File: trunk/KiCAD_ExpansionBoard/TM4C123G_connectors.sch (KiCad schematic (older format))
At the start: 0 parts

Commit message: Creation of project (sheets) structure and add some library schematic component (transceiver.lib, headers, etc.)
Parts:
- added J1: TI_BOOSTER_40_J1, ~, symbol TI_BOOSTER_40_J1
- added J2: TI_BOOSTER_40_J2, ~, symbol TI_BOOSTER_40_J2
- added J3: TI_BOOSTER_40_J3, ~, symbol TI_BOOSTER_40_J3
- added J4: TI_BOOSTER_40_J4, ~, symbol TI_BOOSTER_40_J4
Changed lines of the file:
@@
 EESchema Schematic File Version 2
+LIBS:boosterpack
 LIBS:power
 LIBS:device
@@
 LIBS:contrib
 LIBS:valves
+LIBS:transceiver
 LIBS:TM4C123G_CommExpBoard-cache
 EELAYER 27 0
@@
 Date "9 jun 2014"
 Rev "0.1"
-Comp "Luca Buccolini, student @ Università Politecnica delle Marche"
+Comp "Luca Buccolini, Student @ Università Politecnica delle Marche"
 Comment1 "Expansion Board for the Texas Instruments TM4C123G Launchpad "
 Comment2 ""
@@
 Comment4 ""
 $EndDescr
+$Comp
+L TI_BOOSTER_40_J1 J1
+U 1 1 5395F11E
+P 10400 1300
+F 0 "J1" H 10350 1950 60  0000 C CNN
+F 1 "TI_BOOSTER_40_J1" H 10400 650 60  0000 C CNN
+F 2 "~" H 10400 1300 60  0000 C CNN
+F 3 "http://www.farnell.com/datasheets/1662126.pdf" H 10400 1300 60  0001 C CNN
+F 4 "Farnell" H 10400 1300 60  0001 C CNN "Supplier 1"
+F 5 "1593464" H 10400 1300 60  0001 C CNN "Supplier 1 P/N"
+F 6 "Multicomp" H 10400 1300 60  0001 C CNN "Producer"
+F 7 "2212S-10SG-85" H 10400 1300 60  0001 C CNN "Producer P/N"
+	1    10400 1300
+	1    0    0    -1
+$EndComp
+$Comp
+L TI_BOOSTER_40_J2 J2
+U 1 1 5395F12D
+P 10400 2900
+F 0 "J2" H 10350 3550 60  0000 C CNN
+F 1 "TI_BOOSTER_40_J2" H 10400 2250 60  0000 C CNN
+F 2 "~" H 10400 2900 60  0000 C CNN
+F 3 "http://www.farnell.com/datasheets/1662126.pdf" H 10400 2900 60  0001 C CNN
+F 4 "Farnell" H 10400 2900 60  0001 C CNN "Supplier 1"
+F 5 "1593464" H 10400 2900 60  0001 C CNN "Supplier 1 P/N"
+F 6 "Multicomp" H 10400 2900 60  0001 C CNN "Producer"
+F 7 "2212S-10SG-85" H 10400 2900 60  0001 C CNN "Producer P/N"
+	1    10400 2900
+	1    0    0    -1
+$EndComp
+$Comp
+L TI_BOOSTER_40_J3 J3
+U 1 1 5395F13C
+P 10400 4550
+F 0 "J3" H 10350 5200 60  0000 C CNN
+F 1 "TI_BOOSTER_40_J3" H 10400 3900 60  0000 C CNN
+F 2 "~" H 10400 4550 60  0000 C CNN
+F 3 "http://www.farnell.com/datasheets/1662126.pdf" H 10400 4550 60  0001 C CNN
+F 4 "Farnell" H 10400 4550 60  0001 C CNN "Supplier 1"
+F 5 "1593464" H 10400 4550 60  0001 C CNN "Supplier 1 P/N"
+F 6 "Multicomp" H 10400 4550 60  0001 C CNN "Producer"
+F 7 "2212S-10SG-85" H 10400 4550 60  0001 C CNN "Producer P/N"
+	1    10400 4550
+	1    0    0    -1
+$EndComp
+$Comp
+L TI_BOOSTER_40_J4 J4
+U 1 1 5395F14B
+P 10400 6150
+F 0 "J4" H 10350 6800 60  0000 C CNN
+F 1 "TI_BOOSTER_40_J4" H 10400 5500 60  0000 C CNN
+F 2 "~" H 10400 6150 60  0000 C CNN
+F 3 "http://www.farnell.com/datasheets/1662126.pdf" H 10400 6150 60  0001 C CNN
+F 4 "Farnell" H 10400 6150 60  0001 C CNN "Supplier 1"
+F 5 "1593464" H 10400 6150 60  0001 C CNN "Supplier 1 P/N"
+F 6 "Multicomp" H 10400 6150 60  0001 C CNN "Producer "
+F 7 "2212S-10SG-85" H 10400 6150 60  0001 C CNN "Producer P/N"
+	1    10400 6150
+	1    0    0    -1
+$EndComp
 $EndSCHEMATC

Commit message: Circuit board schematic complete! TODO: Update schematic according new received specifics: "note-expansionboard_20140623.txt"
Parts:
- added C5: 10n, ~, symbol C
- added C6, C7: 1n, ~, symbol C
- added P10: EB_GPIO0, symbol CONN_4X2
- added P6: CAN, symbol CONN_4
- added P7: UART1, symbol CONN_3X2
- added P8: RS485, symbol CONN_4
- added P9: UART2, symbol CONN_3X2
- added Q2: TSM3457, SOT-26_MD, symbol MOS_P
- added R19: 15k, ~, symbol R
- added R20, R23, R24, R25, R26: 4k7, ~, symbol R
- added R21, R22: 22, ~, symbol R
- added TVS3: SMCJ12CA, DO-214AB_MD, symbol TVS
- J1, J2, J3: Supplier 2 (none) -> Taydaelectronics; Supplier 2 P/N (none) -> A-1053
- J4: Producer (none) -> Multicomp; Producer  Multicomp -> (none); Supplier 2 (none) -> Taydaelectronics; Supplier 2 P/N (none) -> A-1053
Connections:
- net labels added: +12V_BUS, +12V_BUS_UNP, +3.3V_EB, +3.3V_TLP, +5V_TLP, AIN0, AIN1, CAN0_EN, CAN0_RS, CAN0_RX, CAN0_TX, CAN_H, CAN_L, EXT_AIN0, EXT_AIN1, GND, I2C0_SCL, I2C0_SDA, I2C1_SCL, I2C1_SDA, LED_B, LED_G, LED_R, RESET, RFM_CLK, RFM_GPIO0, RFM_GPIO1, RFM_MISO, RFM_MOSI, RFM_NIRQ, RFM_SCLK, RFM_SDN, RFM_SSEL, RS485_A, RS485_B, RS485_RXEN#, RS485_TXEN, SW1, SW2, UART1_CTS, UART1_RTS, UART1_RX, UART1_TX, UART2_RST, UART2_RX, UART2_TREQ, UART2_TX, UART3_RX, UART3_TX, V_AN_MONITOR
- wire segments 0 -> 114
- no-connect marks 0 -> 6
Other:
- note added: "4x Stackable 10 pin headers"
- note added: "ADC input: generic \nanti-aliasing filter"
- note added: "CAN connector & \npower supply rail"
- note added: "Divider ratio=0.2541\n"
- note added: "I2C: generic \npull-up resistor"
- note added: "RS-485 connector &\npower supply rail"
- note added: "Spare function 4x2 male header"
- note added: "Transient & reverse polarity protections\nof power supply rail\n"
- note added: "UART1 3x2 male header"
- note added: "UART2 3x2 male header"
- note added: "if order skackable 10 pins header, \nyou can remove the four I2C pins \non this header (EB_GPIO0)"

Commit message: -Unito le due linee a 3.3V e riposizionato Q1 che ora va ad interrompere la linea di alimentazione a 3.3V dello switching quando è presente la +5V_TLP (USB). In serie al gate ho messo R8 da 120 ohm e ho lasciato R7 da 10k di pull-down.
-Ho messo un NPN, Q3, che ha al suo interno un partitore da 22k + 47k; è pilotato dalla +5V_TLP ed ho messo R1 verso +12V_BUS che mantiene attivo lo switching a meno che non sia presente la +5V_TLP (Q3 ON). Infine ho posizionato il led a monte del PMOS.

-Per la protezione dalle sovratensioni sulla +5V_TLP ho inserito, all'ingesso, TVS4 che è bidirezionale con tensione di lavoro a 5V e tensione di breakdown di 5.8V (min).

-Rimosse tutte le resistenze di pull-up nei transceiver: ne avevano alcune già internamente.

-Sostituiti gli header-jumper per i terminatori e la rete di fail-safe biasing con un SPDT (SW1), ed un 4PDT (SW2).

In serie al pin RS del transceiver ho messo una 10k.

Pull-up da 10k su SDN dell'RF module
 
Ho inserito un secondo TP P1, ANT_GND che posizionerò vicino al primo, P5, ANT_C per il collegamento dell'antenna.

-MISURA DELLA TENSIONE DI BUS: V_AN_MONITOR: ho ricalcolato i valori di R19 e R20 per ottenere un divider ratio pari a 6.236 circa anziché 6.206 come indicato. La tensione di fondo scala sarà vicina ai 20 V.

-Il TVS3 (SMCJ12CA) indicato è bidirezionale (DS: http://www.farnell.com/datasheets/1794554.pdf), così ho corretto il simbolo mettendone uno appropriato.

-Sostituito lo "spare-function header" da 2x4 pin con uno 2x5 pin reimpostando pin-out come indicato, comprensivo di massa ed alimentazione.
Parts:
- removed P10: EB_GPIO0, symbol CONN_4X2
- removed TVS3: SMCJ12CA, DO-214AB_MD, symbol TVS
- added P10: EB_GPIO0, ~, symbol CONN_5X2
- added TVS3: SMCJ12CA, SMC, symbol BID_TVS
- added TVS4: ESD5B5.0ST1G, SOD-523_MD, symbol BID_TVS
- J1, J2, J3, J4: Descriprion (none) -> STACKABLE HEADER 10 PINS 2.54MM
- P7, P9: Descriprion (none) -> 3x2 male header
- R19: value 15k -> 10k; Descriprion RESISTORE, 15K, 0.125W, 1%, 0805, SMD -> RESISTOR, 0805, 10K, 1%, ANTI SULFUR; Producer VISHAY DRALORIC -> MULTICOMP; Producer P/N CRCW080515K0FKEA -> MCMR08X1002FTL; Supplier 1 P/N 1652920 -> 2073607
- R20: value 4k7 -> 1k91; Descriprion RESISTOR, 0805, 4K7, 1%, ANTI SULFUR -> RESISTORE, 0805, 1K91, 1%; Producer MULTICOMP -> VISHAY DRALORIC; Producer P/N MCMR08X4701FTL -> CRCW08051K91FKEA; Supplier 1 P/N 2073779 -> 2138942
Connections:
- net labels added: +3.3V, +5V
- net labels removed: +3.3V_EB, +3.3V_TLP, +5V_TLP
- wire segments 114 -> 122
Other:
- note added: "Divider ratio=6.236\n"
- note added: "Spare function 5x2 male header"
- note added: "Transient protections\nof +5V (USB) supply rail\n"
- note removed: "Divider ratio=0.2541\n"
- note removed: "Spare function 4x2 male header"
- moved on the sheet: P6, P8, Q2

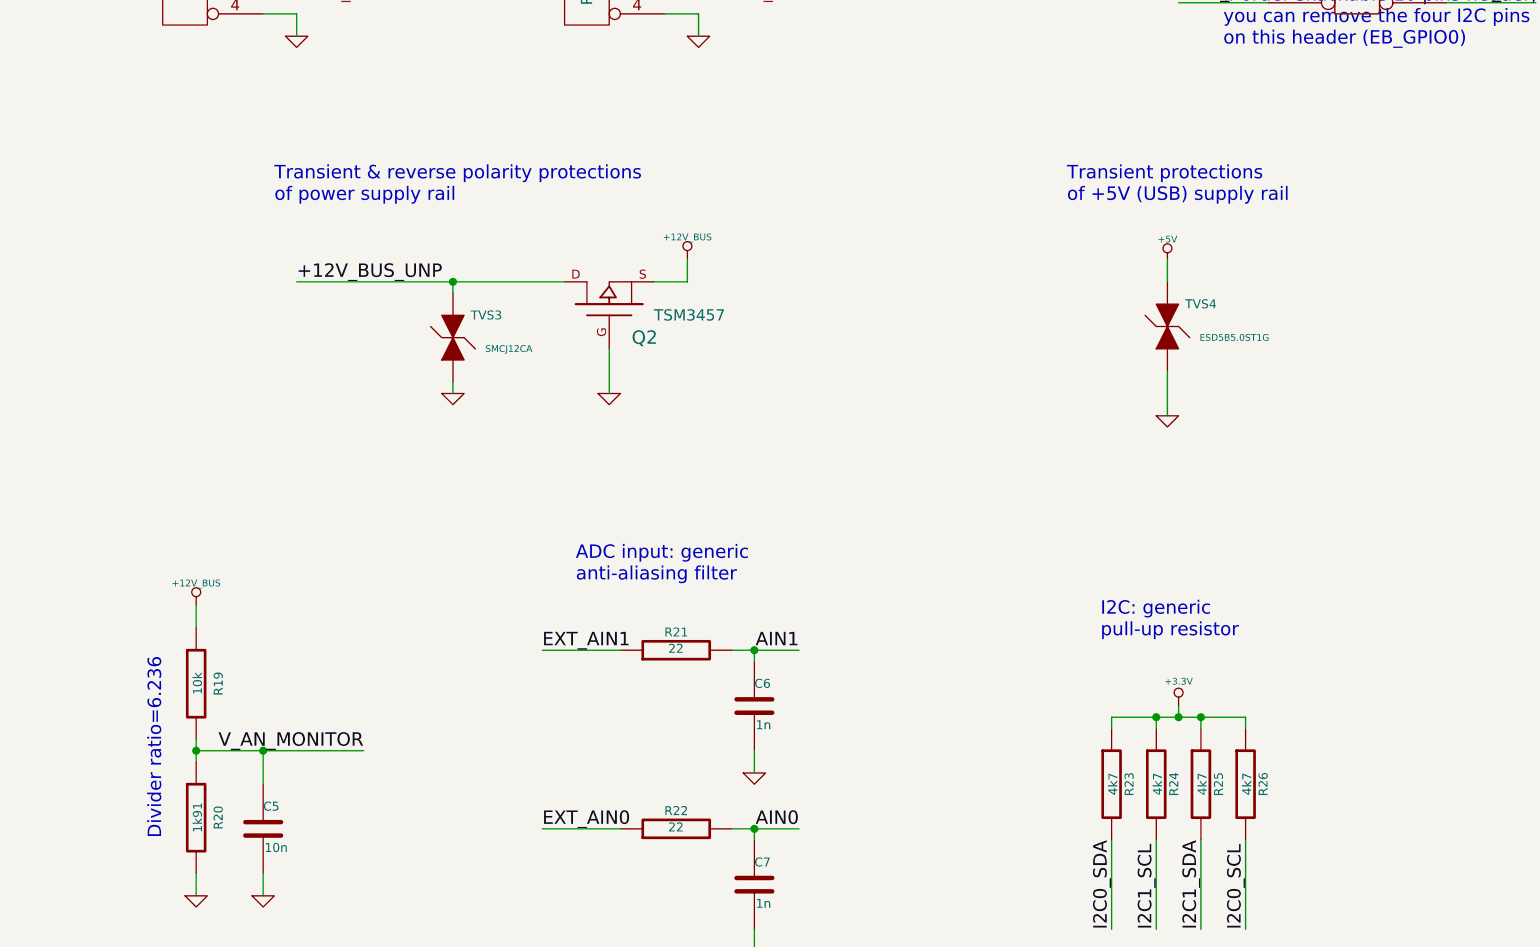
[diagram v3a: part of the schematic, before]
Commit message: -Eliminata R7> con l-aggiunta di Q3 ora il pull down [ incorporato in esso, un-altro sprecher' solo corrente -Aumentate R1 e R18 a 100k -Modificata la connessione di SW2 per minimizzare la capacit' sul bus
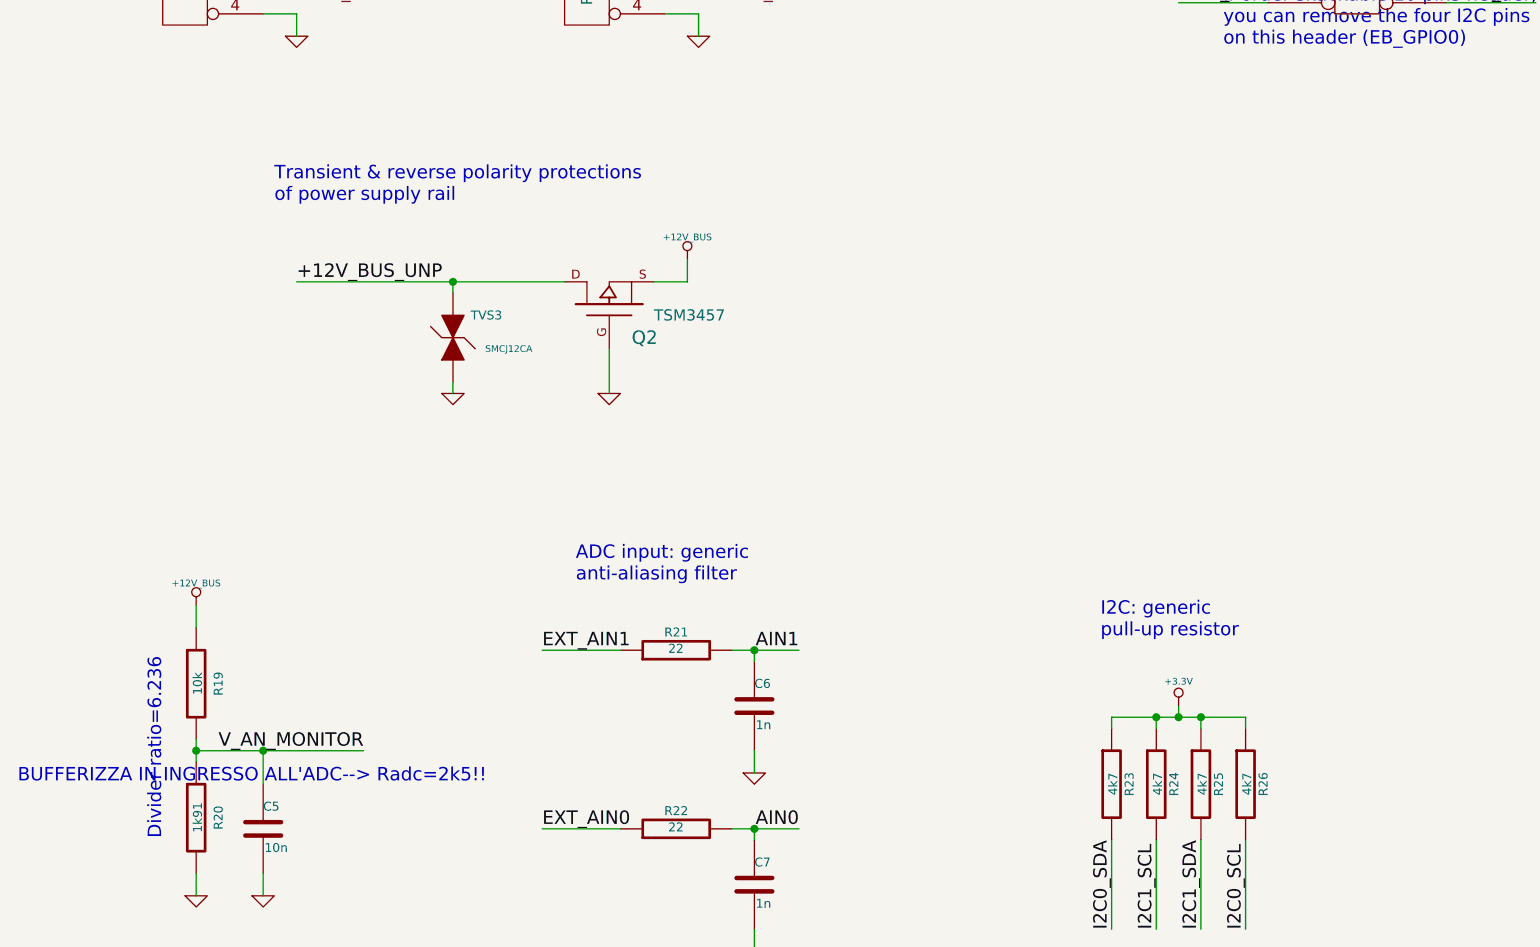
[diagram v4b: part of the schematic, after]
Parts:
- removed TVS4: ESD5B5.0ST1G, SOD-523_MD, symbol BID_TVS
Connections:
- wire segments 122 -> 120
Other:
- note added: "BUFFERIZZA IN INGRESSO ALL'ADC--> Radc=2k5!!"
- note removed: "Transient protections\nof +5V (USB) supply rail\n"
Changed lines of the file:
@@
 Sheet 3 3
 Title "TM4C123G Communication Expansion Board"
-Date "3 jul 2014"
-Rev "0.2"
+Date "11 jul 2014"
+Rev "0.3"
 Comp "Luca Buccolini, Student @ Università Politecnica delle Marche"
 Comment1 "Expansion Board for the Texas Instruments TM4C123G Launchpad "
@@
 $EndComp
 $Comp
-L +5V #PWR047
-U 1 1 53B3C4D5
-P 5500 4450
-F 0 "#PWR047" H 5500 4540 20  0001 C CNN
-F 1 "+5V" H 5500 4540 30  0000 C CNN
-F 2 "~" H 5500 4450 60  0000 C CNN
-F 3 "~" H 5500 4450 60  0000 C CNN
-	1    5500 4450
-	1    0    0    -1
-$EndComp
-$Comp
-L +3.3V #PWR048
+L +3.3V #PWR047
 U 1 1 53B3C4E8
 P 5850 2850
-F 0 "#PWR048" H 5850 2810 30  0001 C CNN
+F 0 "#PWR047" H 5850 2810 30  0001 C CNN
 F 1 "+3.3V" H 5850 2960 30  0000 C CNN
 F 2 "~" H 5850 2850 60  0000 C CNN
@@
 	9050 4100 9050 4000
 $Comp
-L +5V #PWR049
+L +5V #PWR048
 U 1 1 53B43EA6
 P 9050 4000
-F 0 "#PWR049" H 9050 4090 20  0001 C CNN
+F 0 "#PWR048" H 9050 4090 20  0001 C CNN
 F 1 "+5V" H 9050 4090 30  0000 C CNN
 F 2 "~" H 9050 4000 60  0000 C CNN
 F 3 "~" H 9050 4000 60  0000 C CNN
 	1    9050 4000
-	1    0    0    -1
-$EndComp
-Wire Wire Line
-	5500 4550 5500 4450
-Wire Wire Line
-	5500 5150 5500 4950
-$Comp
-L GND #PWR050
-U 1 1 53B44049
-P 5500 5150
-F 0 "#PWR050" H 5500 5150 30  0001 C CNN
-F 1 "GND" H 5500 5080 30  0001 C CNN
-F 2 "" H 5500 5150 60  0000 C CNN
-F 3 "" H 5500 5150 60  0000 C CNN
-	1    5500 5150
-	1    0    0    -1
-$EndComp
-$Comp
-L BID_TVS TVS4
-U 1 1 53B4413C
-P 5500 4750
-F 0 "TVS4" H 5650 4850 40  0000 C CNN
-F 1 "ESD5B5.0ST1G" H 5800 4700 30  0000 C CNN
-F 2 "SOD-523_MD" V 5200 4750 60  0001 C CNN
-F 3 "http://www.onsemi.com/pub/Collateral/ESD5B5.0ST1G.PDF" H 5750 4800 60  0001 C CNN
-F 4 "Farnell" H 5500 4750 60  0001 C CNN "Supplier 1"
-F 5 "2317513" H 5500 4750 60  0001 C CNN "Supplier 1 P/N"
-F 6 "ON SEMICONDUCTOR" H 5500 4750 60  0001 C CNN "Producer"
-F 7 "ESD5B5.0ST1G" H 5500 4750 60  0001 C CNN "Producer P/N"
-F 8 "ESD PROTECTION DIODE, 5V, SOD-523-2" H 5500 4750 60  0001 C CNN "Descriprion"
-	1    5500 4750
 	1    0    0    -1
 $EndComp
@@
 	1    0    0    -1
 $EndComp
-Text Notes 5050 4200 0    60   ~ 0
-Transient protections\nof +5V (USB) supply rail\n
+Text Notes 350  6800 0    60   ~ 0
+BUFFERIZZA IN INGRESSO ALL'ADC--> Radc=2k5!!
 $EndSCHEMATC
